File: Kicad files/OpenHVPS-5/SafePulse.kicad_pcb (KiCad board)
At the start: 4 copper layers, 40.6 x 20.8 mm, 90 parts, among them J1 Conn_01x03_Male, Q1 FQT7N10L, Q2 BC846A, Q3 MMBT3906, Q4 MMBT3906, U1 TS4061AILT-1.25, U2 74HC14, U3 TLV27L1IDBVT, U33 MAX9910EXK+T, U4 CD14538BM

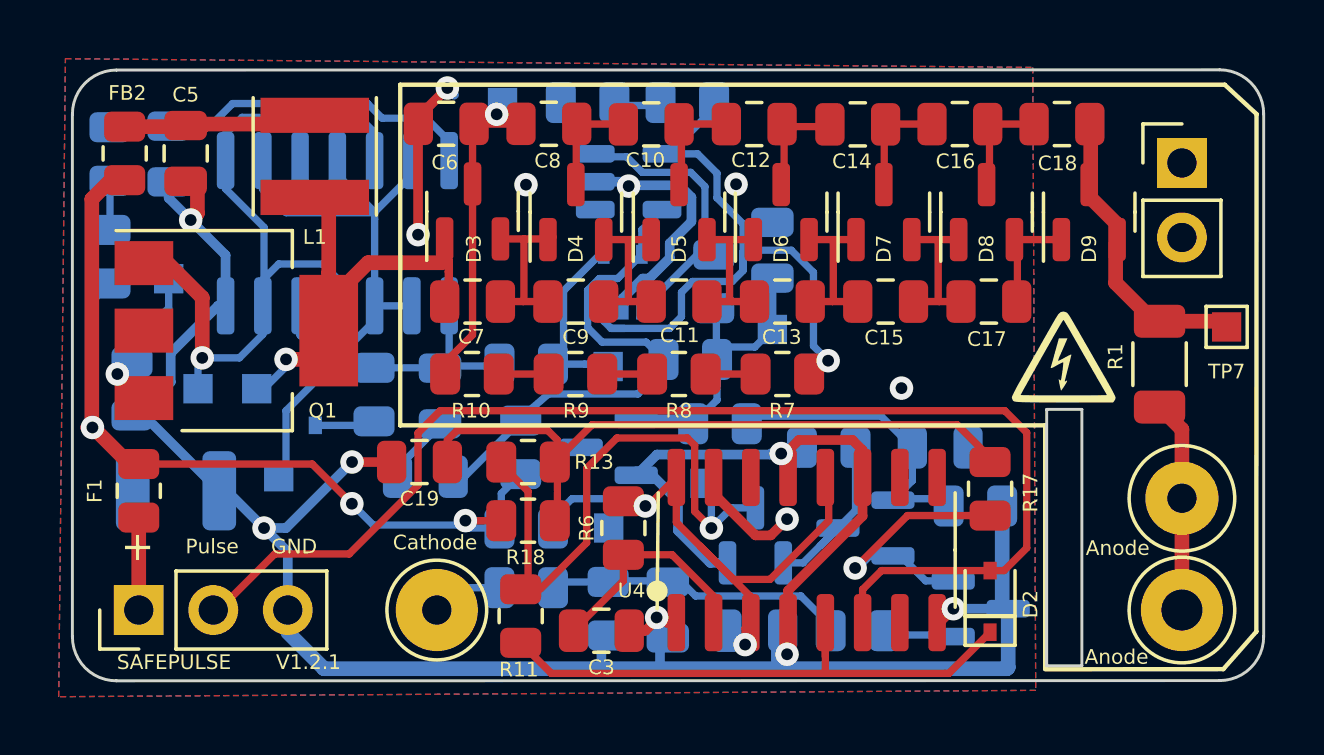
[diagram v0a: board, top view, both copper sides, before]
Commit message: Added parts list for JLPCB
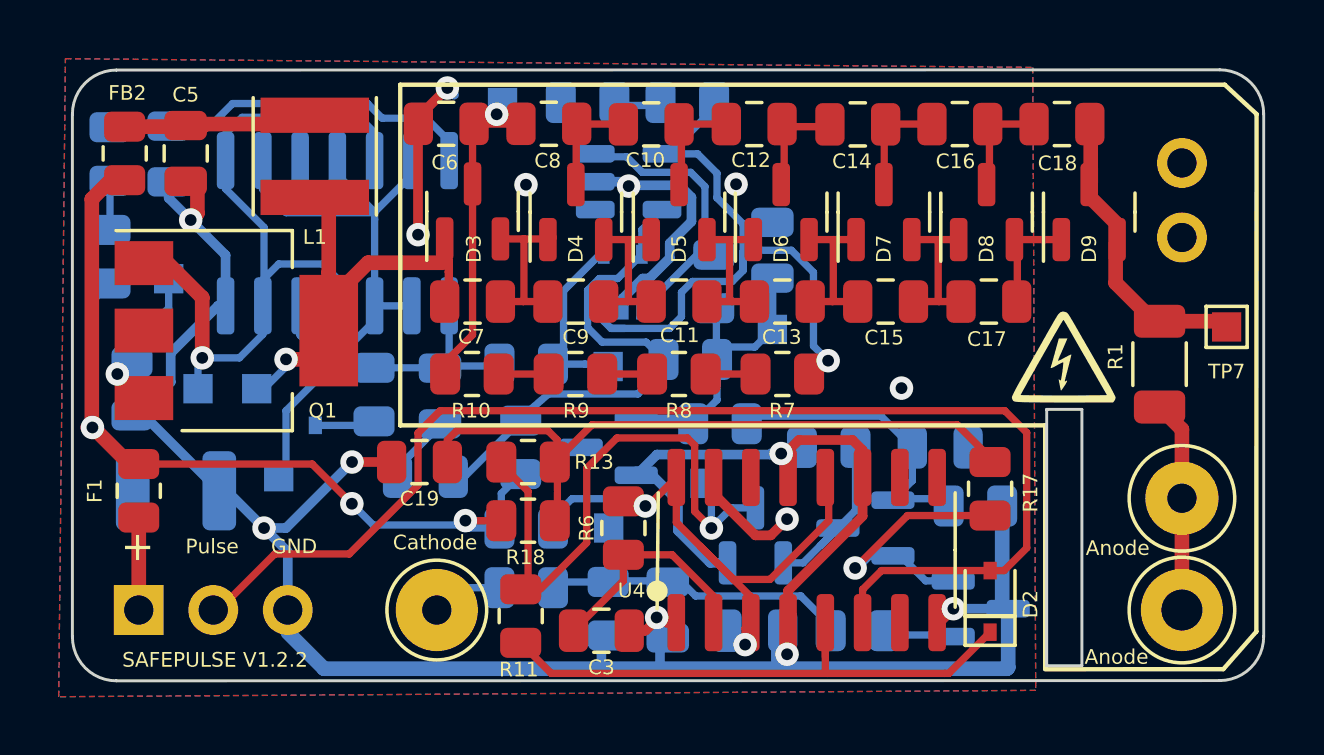
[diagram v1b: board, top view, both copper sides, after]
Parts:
- R1: value 4.7M -> 4.99M
- R15: value 392k -> 220k
- R24: value 33k -> 22k
- U3: value TLV27L1IDBVT -> TLV27L1DBVT
- turned R27 to -90 degrees
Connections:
- R27 pad 1: +1V2 -> Net-(R27-Pad1)
- R27 pad 2: Net-(R27-Pad2) -> +1V2
- U3 pad 3: Net-(R27-Pad2) -> Net-(R27-Pad1)
- U33 pad 1: Net-(R27-Pad2) -> Net-(R27-Pad1)
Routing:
- net Net-(R27-Pad2): track 9.47 -> 0.00 mm
- net Net-(R27-Pad1): track 0.00 -> 9.47 mm
- net Net-(U4-Pad12): vias 2 -> 0
- net (no net): vias 0 -> 2
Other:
- board text added: "SAFEPULSE V1.2.2"
- board text removed: "SAFEPULSE V1.2.1"
